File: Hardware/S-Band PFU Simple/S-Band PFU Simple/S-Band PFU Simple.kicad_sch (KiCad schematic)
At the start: 16 parts, among them J1 2057-RF2-152-T-00-50-G-HDW-ND, J2 2057-RF2-152-T-00-50-G-HDW-ND, J3 2057-RF2-152-T-00-50-G-HDW-ND, J4 Conn_01x02_Pin, U1 SKY13347-360LF, U2 AZ1117-3.3

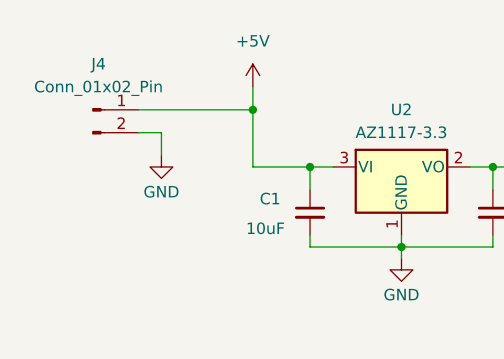
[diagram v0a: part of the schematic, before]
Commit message: Generating Gerbers for PFU
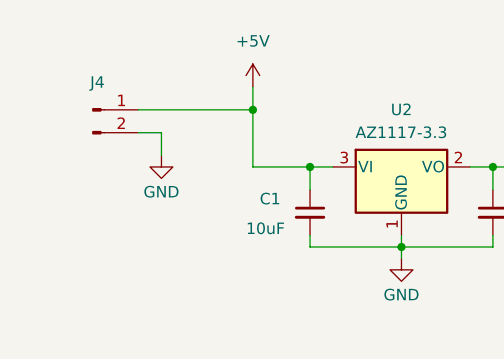
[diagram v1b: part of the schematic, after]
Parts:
- J4: value Conn_01x02_Pin -> 61300211121; Digikey (none) -> 732-5315-ND; MPN (none) -> 61300211121; Manufacturer (none) -> Würth Elektronik
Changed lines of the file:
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@@
 		(on_board yes)
 		(dnp no)
-		(fields_autoplaced yes)
 		(property "Reference" "J4"
-			(at 20.955 22.86 0)
+			(at 20.828 24.892 0)
 			(effects
 				(font
@@
 			)
 		)
-		(property "Value" "Conn_01x02_Pin"
+		(property "Value" "61300211121"
 			(at 20.955 25.4 0)
 			(effects
@@
 					(size 1.27 1.27)
 				)
+				(hide yes)
 			)
 		)
@@
 			)
 		)
-		(property "Description" "Generic connector, single row, 01x02, script generated"
+		(property "Description" "CONN HEADER VERT 2POS 2.54MM"
 			(at 20.32 27.94 0)
 			(effects
+				(font
+					(size 1.27 1.27)
+				)
+				(hide yes)
+			)
+		)
+		(property "Digikey" "732-5315-ND"
+			(at 20.32 27.94 0)
+			(effects
+				(font
+					(size 1.27 1.27)
+				)
+				(hide yes)
+			)
+		)
+		(property "MPN" "61300211121"
+			(at 20.32 27.94 0)
+			(effects
+				(font
+					(size 1.27 1.27)
+				)
+				(hide yes)
+			)
+		)
+		(property "Manufacturer" "Würth Elektronik"
+			(at 20.32 27.94 0)
+			(effects

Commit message: fixed switch
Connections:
- net GND: now also U1.9 (GND)
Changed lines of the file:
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@@
 		(pin "5"
+		)
+		(pin "9"
 		)
 		(instances
